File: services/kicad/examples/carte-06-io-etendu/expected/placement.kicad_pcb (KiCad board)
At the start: 2 copper layers, 80 x 60 mm, 35 parts, among them J1 IN_5V, J10 IO0, J11 IO1, J2 SWD, U1 STM32F103C8T6, U2 AMS1117-3.3

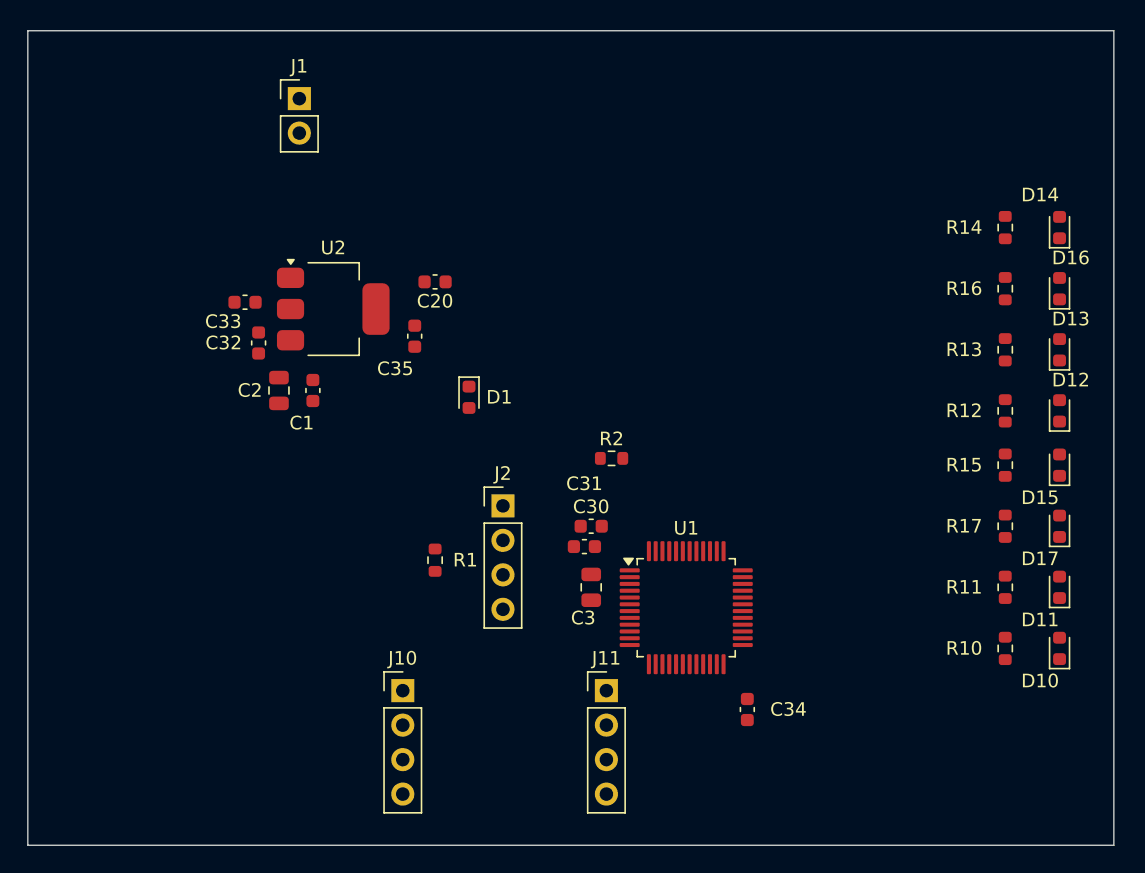
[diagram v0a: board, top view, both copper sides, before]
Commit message: test(examples): quatre cartes livrées plus petites — contour resserré mesuré sur le banc (D-2026-09-13-c A)
Banc rejoué en taille heuristique (phase 1 puis phase 2 à placement gelé) :
carte-01 25x20 -> 24,8x17 (84 % de surface), carte-04 60x45 -> 45x44,8
(75 %), carte-06 80x60 -> 65,2x59,8 (81 %), carte-07 110x80 -> 99,5x79,8
(90 %) — toutes 100 % routées, 0 erreur DRC (vérifié en local), rendus 3D
régénérés. Gain nul sur les cartes denses (le génétique remplit la carte) ;
08 et 09 non livrées (dispersion du routage, surface inchangée) ; carte-11
non livrée (carte d'escalade). Tableau complet dans docs/DECISIONS.md.

Co-Authored-By: Claude Fable 5.1 <noreply@anthropic.com>
Claude-Session: https://claude.ai/code/session_01TnMqm4La2CxQHHB5K8aSSV
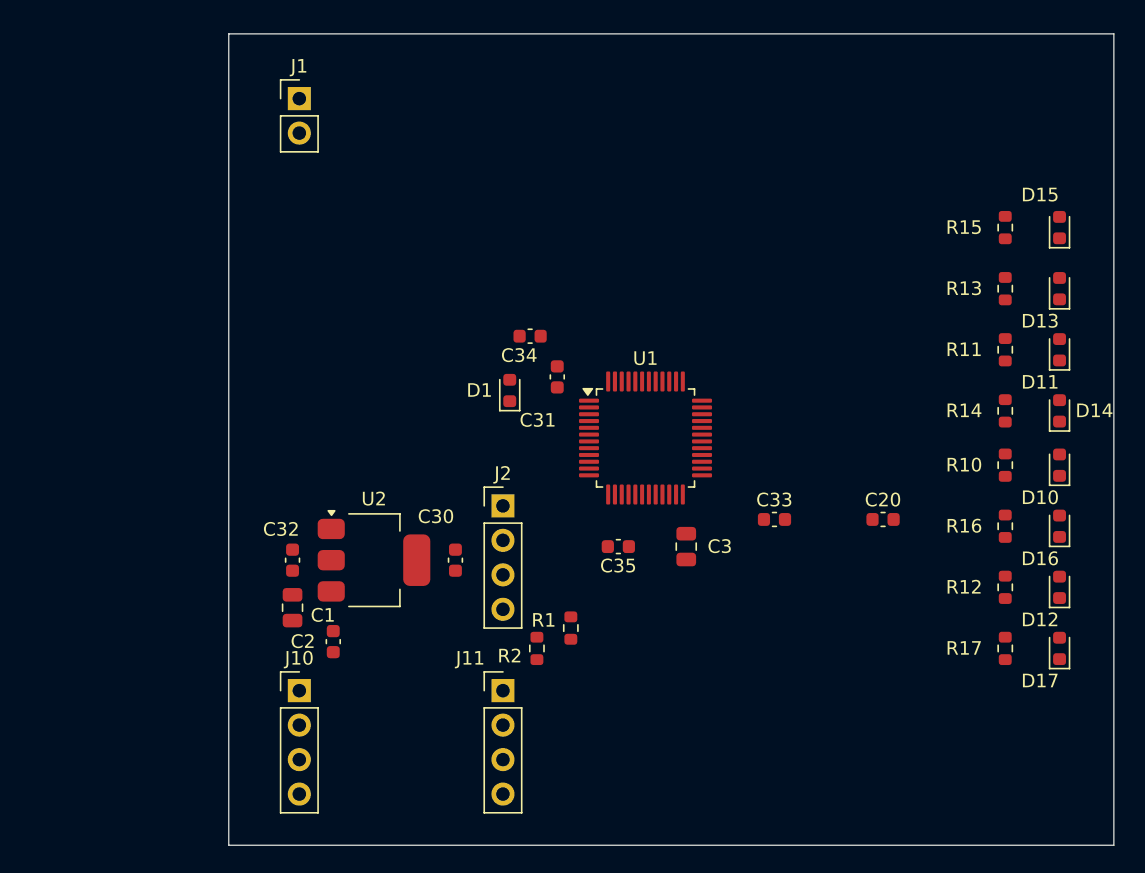
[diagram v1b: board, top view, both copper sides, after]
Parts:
- moved C33 42.2 mm to (163.5, 111.0), turned to 0 degrees
- moved C20 37.4 mm to (171.5, 111.0), turned to 0 degrees
- moved C34 31.8 mm to (145.5, 97.5), turned to 180 degrees
- moved C35 21.6 mm to (152.0, 113.0), turned to 180 degrees
- moved U2 18.7 mm to (134.0, 114.0)
- moved C2 18.6 mm to (131.0, 120.0)
- moved D11 17.5 mm to (184.5, 98.5)
- moved D15 17.5 mm to (184.5, 89.5)
- moved D16 17.5 mm to (184.5, 111.5)
- moved R11 17.5 mm to (180.5, 98.5)
- moved R15 17.5 mm to (180.5, 89.5)
- moved R16 17.5 mm to (180.5, 111.5)
- moved C32 16.2 mm to (128.0, 114.0)
- moved C1 16.0 mm to (128.0, 117.5)
- moved R2 15.0 mm to (146.0, 120.5), turned to 90 degrees
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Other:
- board size 80 x 60 mm -> 65.2 x 59.8 mm

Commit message: chore(banc): relivrer carte-03 et carte-06 compactes apres le correctif des angles
Rejeu complet place -> route des dix cartes par HTTP, code de #223/#224.

  carte-03  50 x 35     -> 27,8 x 19,8   0 erreur · 0 manquante
            (12 erreurs · 9 manquantes le matin, avant #224)
  carte-06  65,2 x 59,8 -> 48,4 x 36,3   0 erreur · 0 manquante

placement.kicad_pcb et final.kicad_pcb remplaces ensemble ; mesures.json
recompte et rejuge (remesurer_banc.py), cle carte_compacte ; rendus refaits.

Tableau des dix cartes dans BANC_DRIVER_LLM.md. 01/02/04/05 gardent leur
board compact du 20/09 matin (propres). 05 et 09 sortent a 1 erreur
(courtyards_overlap U2 <-> passif voisin), 07/08/10 routent desormais mais
gardent 10 a 18 connexions manquantes : non relivrees.

Co-Authored-By: Claude Fable 5.1 <noreply@anthropic.com>
Claude-Session: https://claude.ai/code/session_01TnMqm4La2CxQHHB5K8aSSV
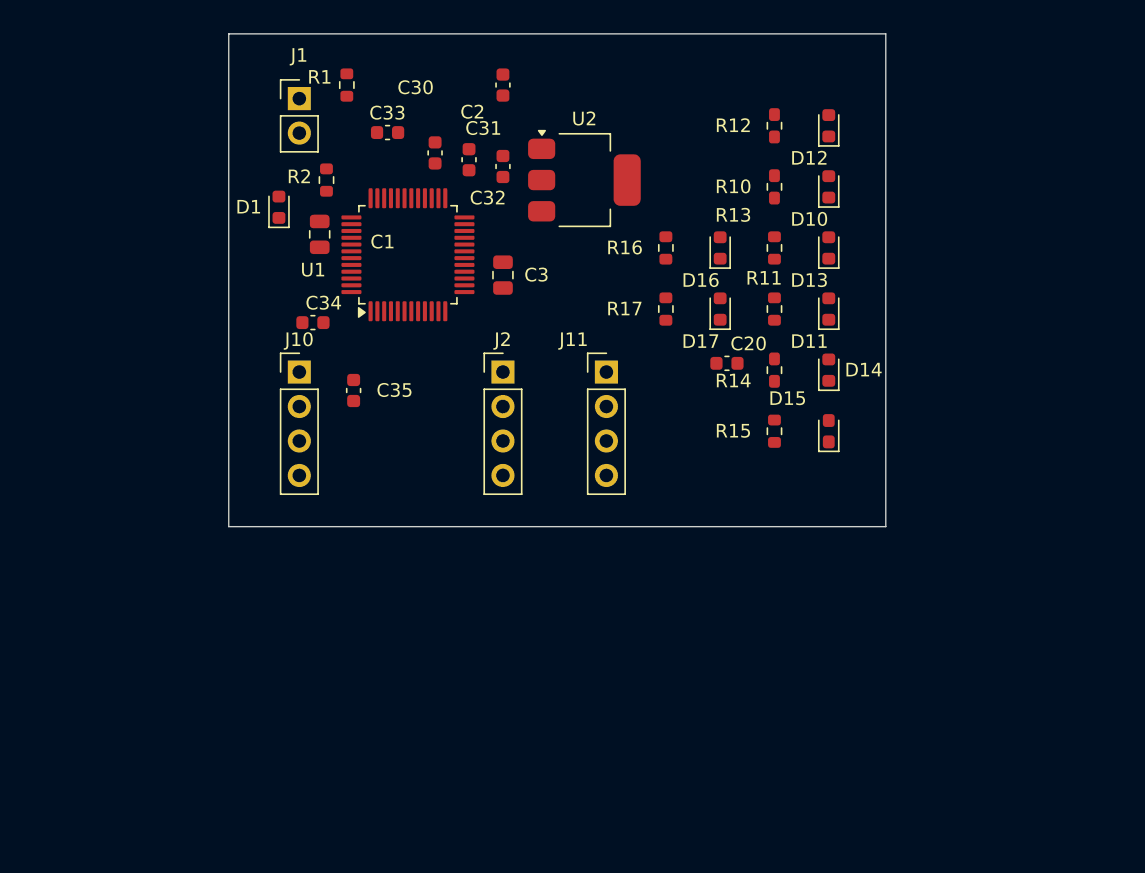
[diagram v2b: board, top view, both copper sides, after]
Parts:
- moved R1 43.3 mm to (132.0, 79.0)
- moved C33 40.3 mm to (135.0, 82.5)
- moved D12 38.0 mm to (167.5, 82.0)
- moved R12 38.0 mm to (163.5, 82.0)
- moved R2 37.8 mm to (130.5, 86.0)
- moved C2 37.2 mm to (143.5, 85.0)
- moved D17 35.4 mm to (159.5, 95.5)
- moved R17 35.4 mm to (155.5, 95.5)
- moved D16 32.3 mm to (159.5, 91.0)
- moved R16 32.3 mm to (155.5, 91.0)
- moved C32 32.2 mm to (141.0, 84.5), turned to 90 degrees
- moved U2 32.0 mm to (149.5, 86.0)
- moved C30 30.0 mm to (138.5, 84.0)
- moved C1 27.6 mm to (130.0, 90.0)
- moved D10 26.6 mm to (167.5, 86.5)
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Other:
- board size 65.2 x 59.8 mm -> 48.4 x 36.3 mm

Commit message: feat(placement): les peripheriques se REPARTISSENT, ils ne s empilent plus
Question de l utilisateur devant le rendu : « c est quoi ce type de placement ? ».
Les composants s entassaient d un seul cote du boitier, etiquettes de
serigraphie l une sur l autre, trois quarts de la couronne vides.

TROIS CAUSES, toutes dans `_poser_les_peripheriques`, toutes la meme faute —
un angle unique pour tout un groupe :

  - les DIRECTS qui visent la meme broche (tous les decouplages d un rail,
    toutes les resistances d un meme signal) recevaient le MEME `angle_vers`
    et le meme rayon de depart ;
  - les SUIVEURS d un meme parent recevaient tous atan2(parent - centre) ;
  - les ISOLES partaient tous de l angle 0.0, c est-a-dire du meme point.

`le_long_du_rayon` ne s ecartait qu une fois la place prise : d ou la file.

REMEDE : `_ecart_en_eventail`. Le PREMIER de chaque groupe garde EXACTEMENT la
direction calculee — c est la topologie, on ne la perd pas pour faire joli — et
les suivants s ecartent symetriquement de 3 x `_PAS_ANGLE_DEG`.
Rien de deja pose ne bouge : seul l ANGLE DE DEPART de la recherche change, et
`le_long_du_rayon` reste seul juge de ce qui est libre.

BANC DES DIX CARTES, contour resserre ET peripheriques repartis :

    carte             demandee    livree         err  manq
    carte-01           25 x 20    20,1 x 13,6     0    0
    carte-02           55 x 40    34,9 x 25,2     0    0
    carte-03           50 x 35    27,6 x 19,9     0    0
    carte-04           60 x 45    36,6 x 29,8     0    0
    carte-05           70 x 50    40,0 x 32,6     0    0
    carte-06           80 x 60    46,5 x 36,4     0    0
    carte-07          110 x 80    47,7 x 38,8     0    0
    carte-08          125 x 95    57,4 x 44,1     0    0
    carte-09          130 x 100   57,8 x 45,2     0    0
    carte-10          140 x 105   59,0 x 45,8     0    0

Dix sur dix, 100 % route. carte-07 gagne 5,5 mm de largeur sur le passage
precedent, carte-06 deux, carte-10 deux. Sur ca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
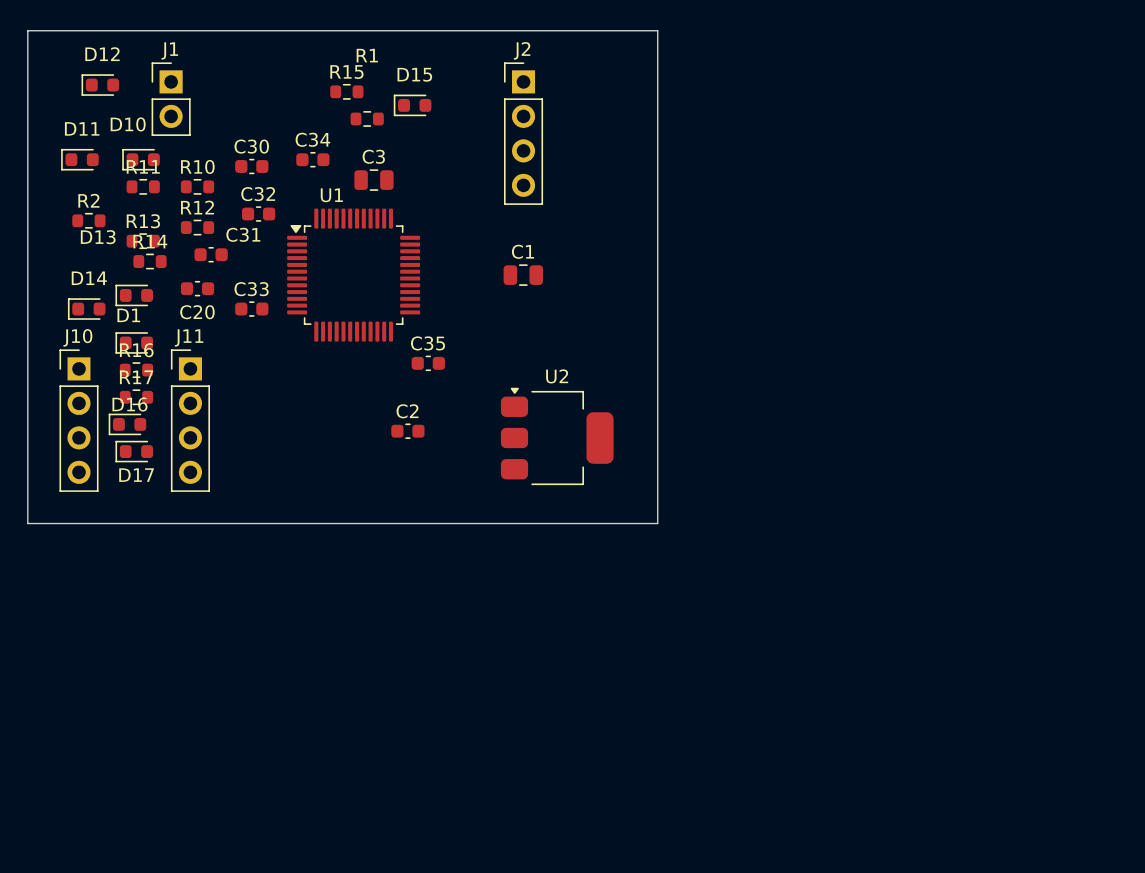
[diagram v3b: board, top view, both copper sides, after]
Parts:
- moved D11 56.1 mm to (112.5, 84.5), turned to 0 degrees
- moved D14 54.7 mm to (113.0, 95.5), turned to 0 degrees
- moved D12 53.6 mm to (114.0, 79.0), turned to 0 degrees
- moved D13 51.1 mm to (116.5, 94.5), turned to 0 degrees
- moved D10 50.5 mm to (117.0, 84.5), turned to 0 degrees
- moved R11 47.4 mm to (117.0, 86.5), turned to 0 degrees
- moved R14 46.7 mm to (117.5, 92.0), turned to 0 degrees
- moved R13 46.5 mm to (117.0, 90.5), turned to 0 degrees
- moved D16 45.4 mm to (116.0, 104.0), turned to 0 degrees
- moved D17 44.3 mm to (116.5, 106.0), turned to 0 degrees
- moved R12 43.2 mm to (121.0, 89.5), turned to 0 degrees
- moved R10 42.5 mm to (121.0, 86.5), turned to 0 degrees
- moved R15 40.2 mm to (132.0, 79.5), turned to 0 degrees
- moved R16 40.0 mm to (116.5, 100.0), turned to 0 degrees
- moved R17 39.5 mm to (116.5, 102.0), turned to 0 degrees
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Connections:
- U1 pad 36: Net-(U1-36) -> PWR_FLAG
- U1 pad 48: Net-(U1-48) -> PWR_FLAG
- U1 pad 9: IO_L5 -> PWR_FLAG
- U2 pad 3: VIN -> PWR_FLAG
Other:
- board size 48.4 x 36.3 mm -> 46.4 x 36.3 mm

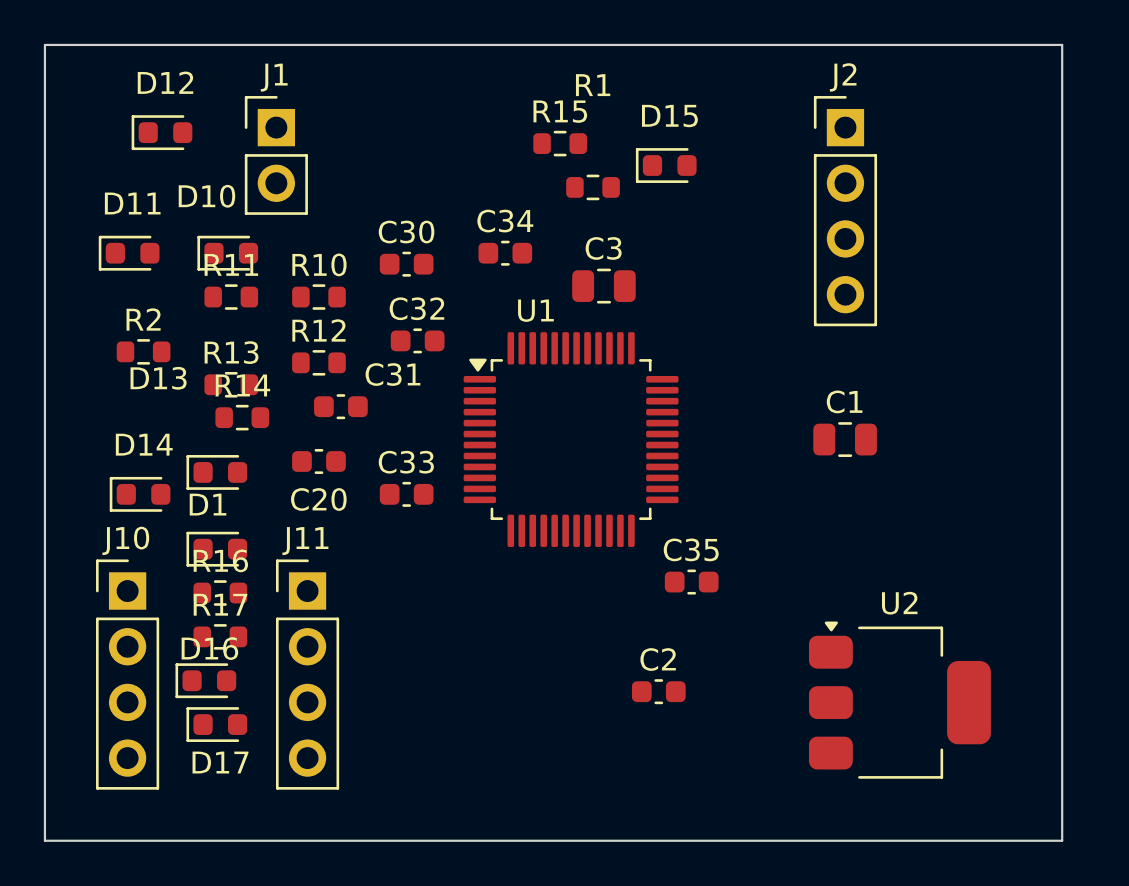
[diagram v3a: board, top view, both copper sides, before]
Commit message: docs(banc): les dix boards du banc du 2026-09-23, service corrige
Artefacts du banc dont le tableau est deja commite : les dix cartes a
100 % route, 0 erreur, 0 connexion manquante, chacune a la taille de son
circuit.

Co-Authored-By: Claude Opus 5 <noreply@anthropic.com>
Claude-Session: https://claude.ai/code/session_01TnMqm4La2CxQHHB5K8aSSV
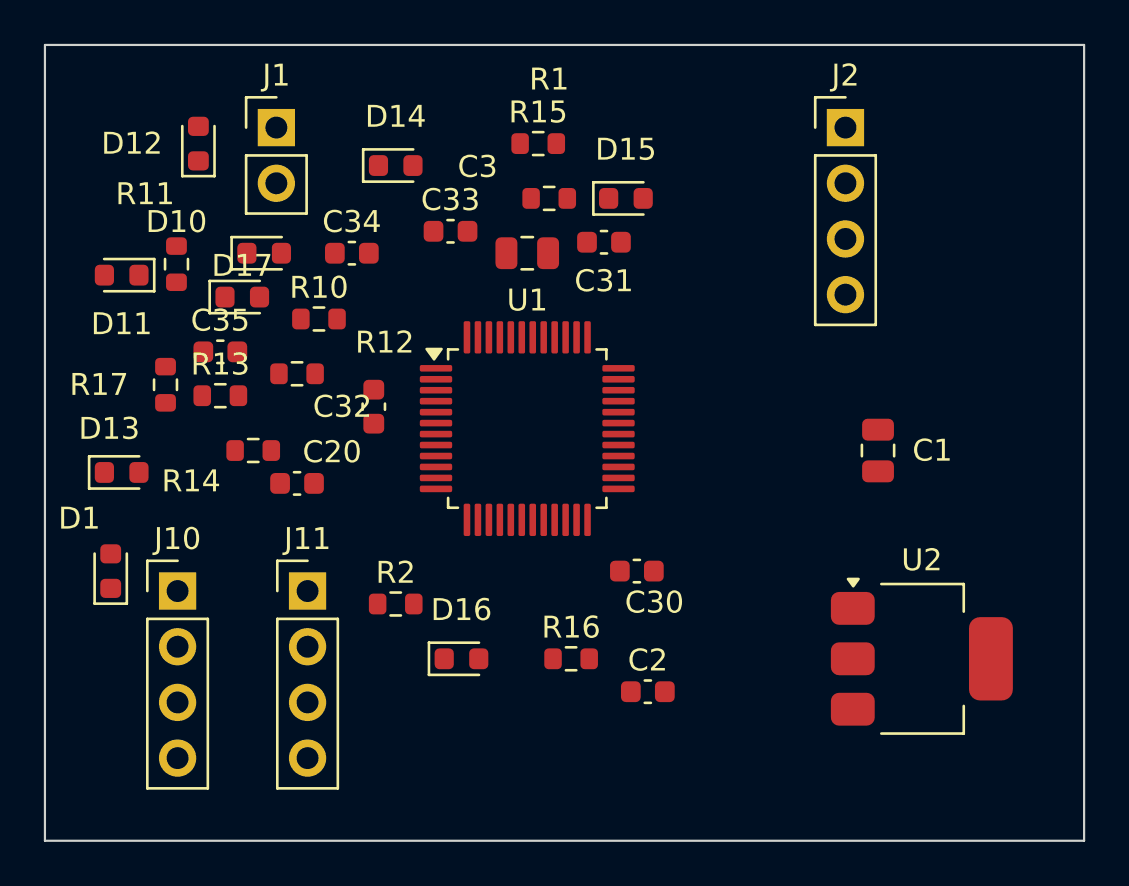
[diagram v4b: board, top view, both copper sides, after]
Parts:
- moved C35 23.9 mm to (116.5, 89.0)
- moved D17 19.5 mm to (117.5, 86.5)
- moved D14 18.9 mm to (124.5, 80.5)
- moved C30 17.5 mm to (135.5, 99.0), turned to 180 degrees
- moved R16 16.3 mm to (132.5, 103.0)
- moved R2 16.3 mm to (124.5, 100.5)
- moved C31 14.2 mm to (134.0, 84.0)
- moved C33 12.2 mm to (127.0, 83.5)
- moved R17 11.8 mm to (114.0, 90.5), turned to 90 degrees
- moved D16 11.5 mm to (127.5, 103.0)
- moved C34 7.00 mm to (122.5, 84.5)
- moved D1 5.10 mm to (111.5, 99.0), turned to 90 degrees
- moved D13 4.50 mm to (112.0, 94.5)
- moved C3 3.81 mm to (130.5, 84.5)
- moved C32 3.61 mm to (123.5, 91.5), turned to 90 degrees
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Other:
- board size 46.4 x 36.3 mm -> 47.4 x 36.3 mm
